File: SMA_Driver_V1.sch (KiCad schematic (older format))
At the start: 70 parts, among them J1 Human_Interface_Tether, J2 RM08V_Conn, Q1 Q_NMOS_GDS, Q2 Q_NMOS_GDS, U1 UDT020A0X3-SRZ, U2 INA332, U3 MCP3208, U4 MicroSD_Breakout_ADF

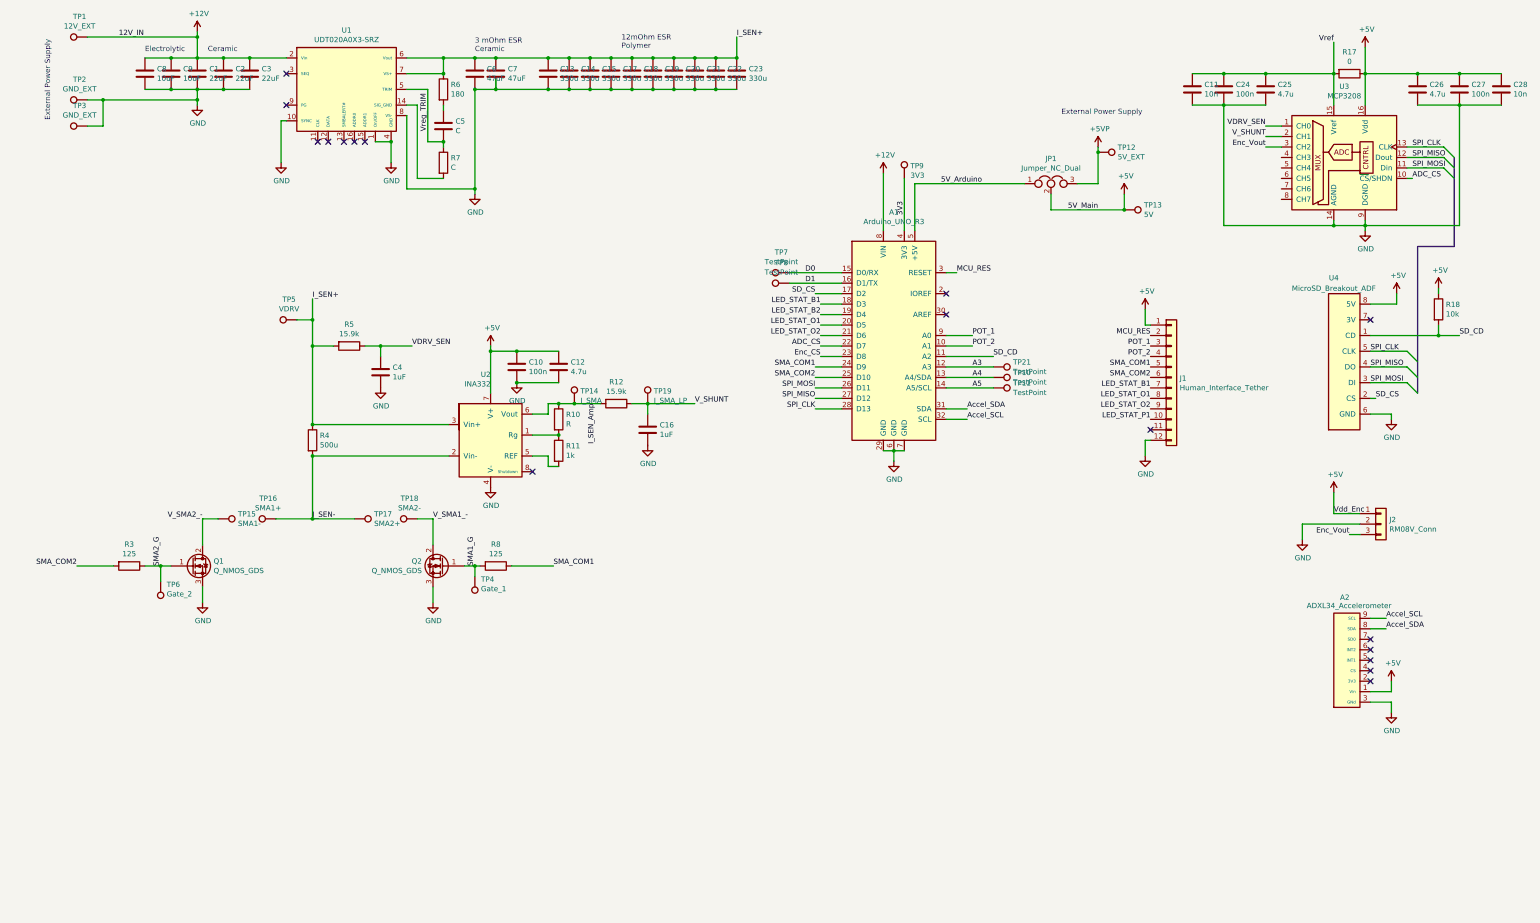
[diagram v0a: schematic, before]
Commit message: fixed notes on 'SMA Driver V1 changes for V2'
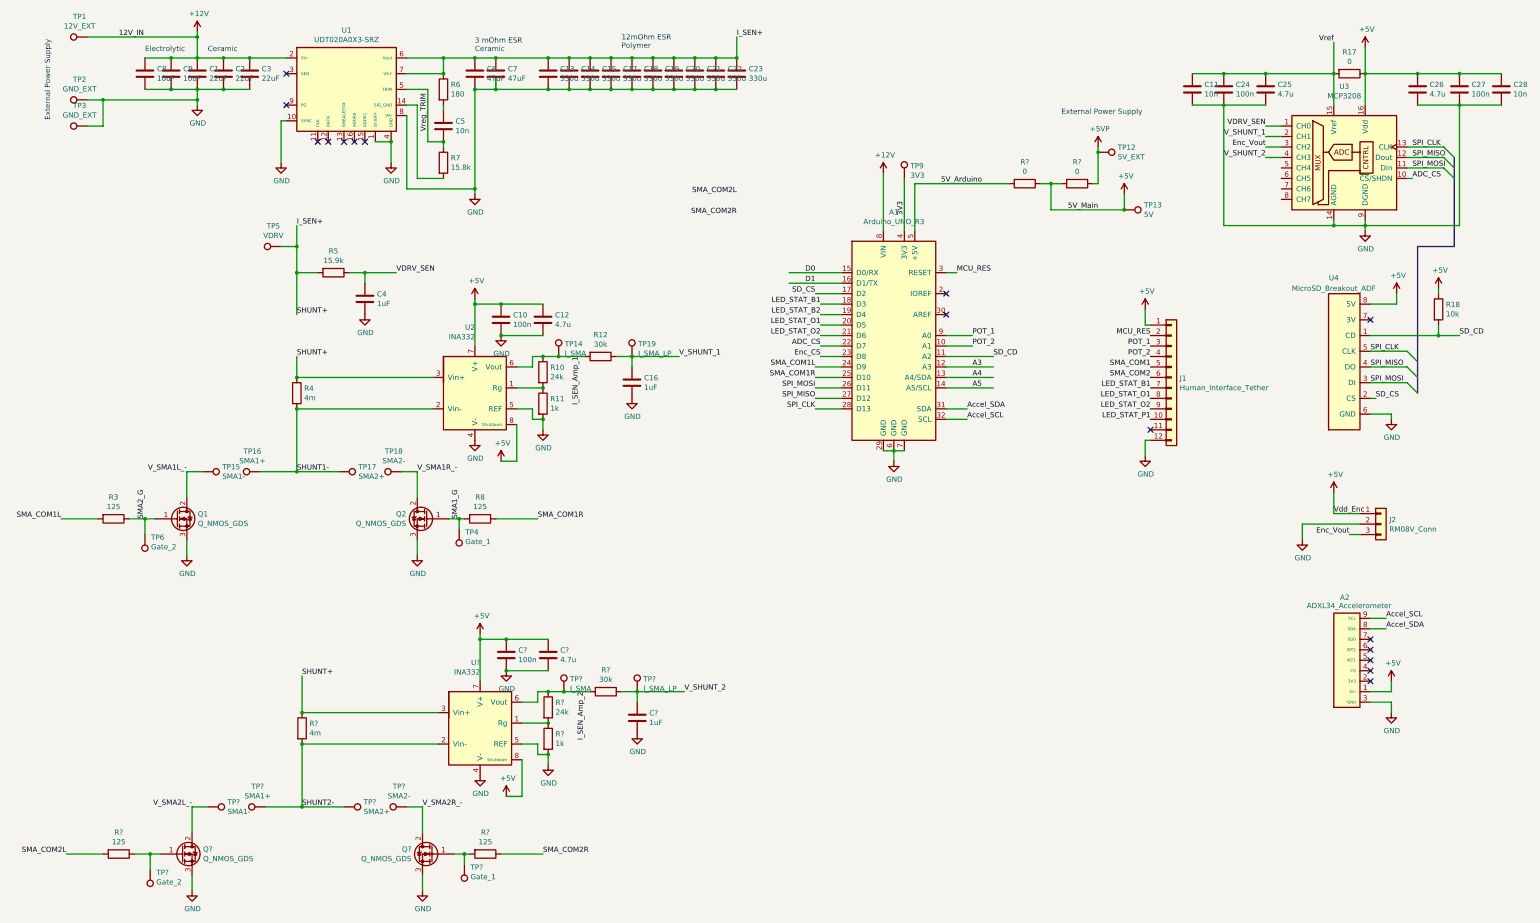
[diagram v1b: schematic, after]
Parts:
- removed JP1: Jumper_NC_Dual, Connector:FanPinHeader_1x03_P2.54mm_Vertical, symbol Device:Jumper_NC_Dual
- removed TP10, TP11, TP21, TP7, TP8: TestPoint, TestPoint:TestPoint_THTPad_D2.0mm_Drill1.0mm, symbol Connector:TestPoint
- added C?: 1uF, Capacitor_SMD:C_0805_2012Metric_Pad1.15x1.40mm_HandSolder, symbol Device:C
- added C?: 100n, Capacitor_SMD:C_0805_2012Metric_Pad1.15x1.40mm_HandSolder, symbol Device:C
- added C?: 4.7u, Capacitor_SMD:C_0805_2012Metric_Pad1.15x1.40mm_HandSolder, symbol Device:C
- added Q? (x2): Q_NMOS_GDS, custom:SO-8FL_v2, symbol Device:Q_NMOS_GDS
- added R? (x2): 0, Resistor_SMD:R_0805_2012Metric, symbol Device:R
- added R?: 4m, Resistor_SMD:R_2512_6332Metric_Pad1.52x3.35mm_HandSolder, symbol Device:R
- added R? (x2): 125, Resistor_SMD:R_0805_2012Metric, symbol Device:R
- added R?: 1k, Resistor_SMD:R_0805_2012Metric, symbol Device:R
- added R?: 24k, Resistor_SMD:R_0805_2012Metric, symbol Device:R
- added R?: 30k, Resistor_SMD:R_0805_2012Metric, symbol Device:R
- added TP?: Gate_2, TestPoint:TestPoint_Loop_D2.60mm_Drill1.6mm_Beaded, symbol Connector:TestPoint
- added TP?: Gate_1, TestPoint:TestPoint_Loop_D2.60mm_Drill1.6mm_Beaded, symbol Connector:TestPoint
- added TP?: I_SMA, TestPoint:TestPoint_Loop_D2.60mm_Drill1.6mm_Beaded, symbol Connector:TestPoint
- added TP?: SMA1-, TestPoint:TestPoint_Plated_Hole_D3.0mm, symbol Connector:TestPoint
- added TP?: SMA2-, TestPoint:TestPoint_Plated_Hole_D3.0mm, symbol Connector:TestPoint
- added TP?: SMA1+, TestPoint:TestPoint_Plated_Hole_D3.0mm, symbol Connector:TestPoint
- added TP?: SMA2+, TestPoint:TestPoint_Plated_Hole_D3.0mm, symbol Connector:TestPoint
- added TP?: I_SMA_LP, TestPoint:TestPoint_Loop_D2.60mm_Drill1.6mm_Beaded, symbol Connector:TestPoint
- added U?: INA332, Package_SO:VSSOP-8_3.0x3.0mm_P0.65mm, symbol SMA_Driver_Components:INA332
- C5: value C -> 10n
- Q1, Q2: footprint custom:SO-8FL -> custom:SO-8FL_v2
- R10: value R -> 24k
- R12: value 15.9k -> 30k
- R4: value 500u -> 4m
- R7: value C -> 15.8k
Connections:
- net +5V: now also U2.8 (Shutdown), C?.1, C?.1, R?.1, R?.2, U?.7 (V+), U?.8 (Shutdown)
- net +5VP: now also R?.1
- net 5V_Arduino: now also R?.2
- net GND: now also R11.2, U2.5 (REF), C?.2, C?.2, C?.2, Q?.3 (S), Q?.3 (S), R?.2, U?.4 (V-), U?.5 (REF)
- net I_SEN+: now also R?.1, U?.3 (Vin+)
- net SMA_COM1: no longer A1.24 (D9), R8.1
- net SMA_COM2: no longer A1.25 (D10), R3.2
- net V_SHUNT_2: now reaches U3.4 (CH3)
- net V_SHUNT_2: now also C?.1, R?.1, TP?.1
- net I_SEN- renamed SHUNT1-
- net I_SEN_Amp renamed I_SEN_Amp_1
- net V_SHUNT renamed V_SHUNT_1
- net V_SMA1_- renamed V_SMA1R_-
- net V_SMA2_- renamed V_SMA1L_-
- new net: Q?.1 (G), R?.1, TP?.1
- new net: Q?.1 (G), R?.2, TP?.1
- new net: R?.1, R?.2, U?.1 (Rg)
- new net I_SEN_Amp_2: R?.1, R?.2, TP?.1, U?.6 (Vout)
- new net SHUNT2-: R?.2, TP?.1, TP?.1, U?.2 (Vin-)
- new net SMA_COM1L: A1.24 (D9), R3.2
- new net SMA_COM1R: A1.25 (D10), R8.1
- new net SMA_COM2L: R?.2
- new net SMA_COM2R: R?.1
- new net V_SMA2L_-: Q?.2 (D), TP?.1
- new net V_SMA2R_-: Q?.2 (D), TP?.1
- no-connect marks 17 -> 16
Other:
- moved on the sheet: C10, C12, C16, C4, Q1, Q2, R10, R11, R12, R3, R4, R5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

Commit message: PCB Rev 2.0 Fixed issues on PCB changes for V2 doc
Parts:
- removed TP17: SMA2+, TestPoint:TestPoint_Plated_Hole_D3.0mm, symbol Connector:TestPoint
- removed TP9: 3V3, TestPoint:TestPoint_THTPad_D2.0mm_Drill1.0mm, symbol Connector:TestPoint
- removed TP?: SMA1+, TestPoint:TestPoint_Plated_Hole_D3.0mm, symbol Connector:TestPoint
- added C32: 10uF, Capacitor_SMD:CP_Elec_5x5.3, symbol Device:C
- added TP22: VREF, TestPoint:TestPoint_Pad_1.5x1.5mm, symbol Connector:TestPoint
- C22: value 330u -> 4.7u; footprint Capacitor_Tantalum_SMD:CP_EIA-7343-43_Kemet-X_Pad2.25x2.55mm_HandSolder -> Capacitor_SMD:C_0805_2012Metric_Pad1.15x1.40mm_HandSolder
- C23: value 330u -> 100n; footprint Capacitor_Tantalum_SMD:CP_EIA-7343-43_Kemet-X_Pad2.25x2.55mm_HandSolder -> Capacitor_SMD:C_0805_2012Metric_Pad1.15x1.40mm_HandSolder
- J1: footprint Connector_Molex:Molex_PicoBlade_53047-2410_1x12_P1.25mm_Vertical -> Connector_Molex:Molex_PicoBlade_53047-2810_1x14_P1.25mm_Vertical; symbol Connector_Generic:Conn_01x12 -> Connector_Generic:Conn_01x14
- J2: footprint Connector_PinHeader_2.54mm:PinHeader_1x03_P2.54mm_Vertical -> Connector_Molex:Molex_PicoBlade_53047-0610_1x03_P1.25mm_Vertical
- gave numbers to parts that had none: 21
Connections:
- net A3 is gone; now on net SD_CD: A1.12 (A3)
- net LED_STAT_P1 is gone; now on net SMA_H2_R: J1.10 (Pin_10)
- net SMA_COM2 is gone; now on net SMA_H1_R: J1.6 (Pin_6)
- net SMA_COM2L is gone; now on net SMA_H2_L: R1.2
- net SMA_COM2R is gone; now on net SMA_H2_R: R9.1
- net +12V: now also C22.1, C23.2, C32.1
- net Enc_Vout: now also U3.8 (CH7); no longer U3.3 (CH2)
- net GND: now also C23.1, J1.14 (Pin_14), C32.2; no longer C23.2, J1.12 (Pin_12)
- net I_SEN+: no longer C22.1, C23.1
- net LED_STAT_B1: now also J1.8 (Pin_8); no longer J1.7 (Pin_7)
- net LED_STAT_B2: now also J1.9 (Pin_9)
- net POT_1: now also A1.10 (A1); no longer A1.9 (A0)
- net POT_2: now also A1.11 (A2); no longer A1.10 (A1)
- net SD_CD: no longer A1.11 (A2)
- net SD_CS: now also A1.9 (A0); no longer A1.17 (D2)
- net V_SHUNT_2: now also U3.3 (CH2); no longer U3.4 (CH3)
- net SMA_H2_L: now reaches J1.11 (Pin_11)
- net SMA_H2_L: now also A1.20 (D5)
- net G_H2_L: now reaches Q3.1 (G), R1.1, TP7.1
- net G_H2_R: now reaches Q4.1 (G), R9.2, TP17.1
- net A4 renamed LED_STAT_O
- net LED_STAT_O: now also J1.7 (Pin_7)
- net A5: no longer names the net of A1.14 (A5/SCL)
- net D0: no longer names the net of A1.15 (D0/RX)
- net D1: no longer names the net of A1.16 (D1/TX)
- net Enc_CS: no longer names the net of A1.23 (D8)
- removed net LED_STAT_O1: A1.20 (D5), J1.8 (Pin_8)
- net LED_STAT_O2 renamed SMA_H2_R
- net SMA_H2_R: no longer J1.9 (Pin_9)
- net SHUNT1- renamed I_SEN1-
- net SHUNT2- renamed I_SEN-
- net SMA1_G renamed G_H1_R
- net SMA2_G renamed G_H1_L
- net SMA_COM1 renamed SMA_H1_L
- net SMA_H1_L: now also A1.25 (D10), R3.2
- net SMA_COM1L renamed SMA_H1_R
- net SMA_H1_R: now also R8.1; no longer R3.2
- removed net SMA_COM1R: A1.25 (D10), R8.1
- net V_SMA1L_- renamed V_H1_L-
- net V_SMA1R_- renamed V_H1_R-
- net V_SMA2L_- renamed V_H2_L-
- net V_SMA2R_- renamed V_H2_R-
- net Vref: no longer names the net of C11.1, C24.1, C25.1, R17.2, U3.15 (Vref)
- net Vref: now also TP22.1
- new net LED_STAT_P: A1.17 (D2), J1.12 (Pin_12)
- no-connect marks 16 -> 24
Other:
- moved on the sheet: TP10, TP16

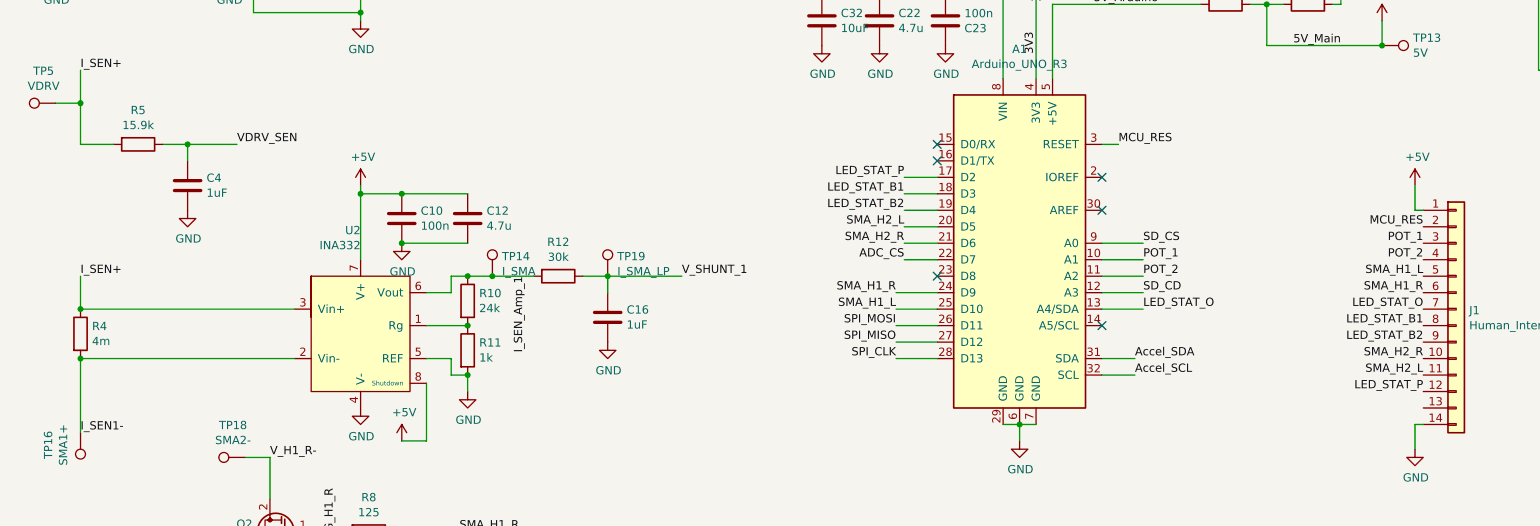
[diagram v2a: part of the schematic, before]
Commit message: added components for button, final draft 1
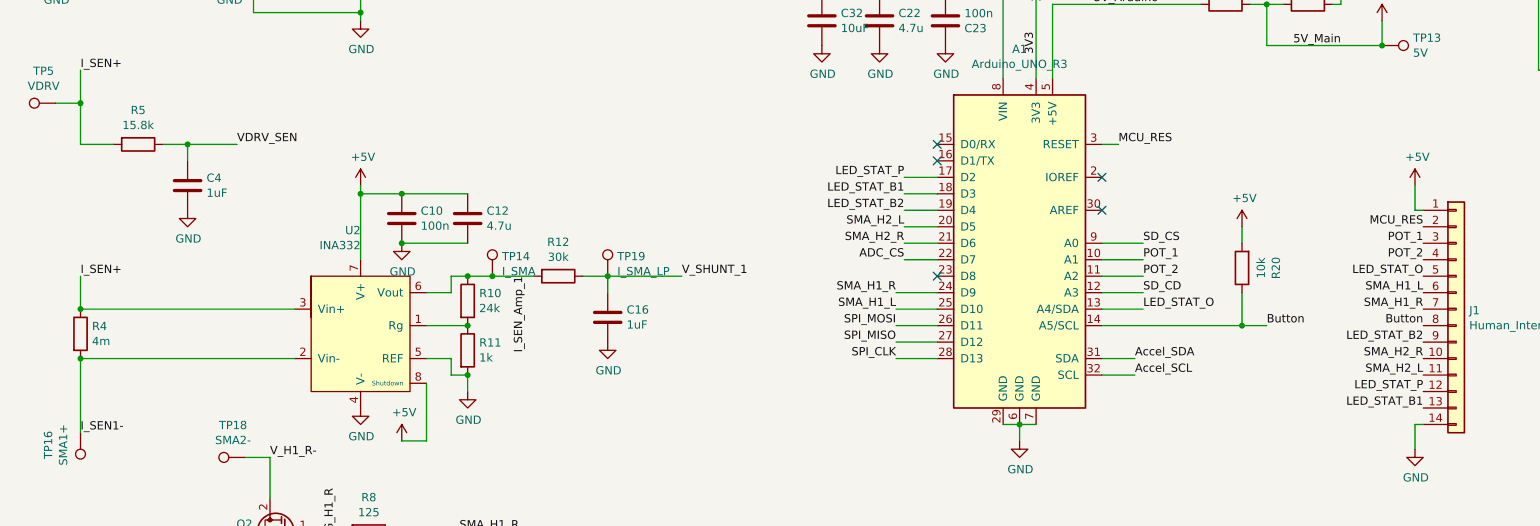
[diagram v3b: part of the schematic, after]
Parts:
- added R20: 10k, Resistor_SMD:R_0805_2012Metric, symbol Device:R
- R5: value 15.9k -> 15.8k
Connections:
- net +5V: now also R20.2
- net LED_STAT_B1: now also J1.13 (Pin_13); no longer J1.8 (Pin_8)
- net LED_STAT_O: now also J1.5 (Pin_5); no longer J1.7 (Pin_7)
- net SMA_H1_L: now also J1.6 (Pin_6); no longer J1.5 (Pin_5)
- net SMA_H1_R: now also J1.7 (Pin_7); no longer J1.6 (Pin_6)
- net Button: now reaches A1.14 (A5/SCL)
- net Button: now also J1.8 (Pin_8), R20.1
- no-connect marks 24 -> 23
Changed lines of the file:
@@
 P 3900 4400
 F 0 "R5" V 3693 4400 50  0000 C CNN
-F 1 "15.9k" V 3784 4400 50  0000 C CNN
+F 1 "15.8k" V 3784 4400 50  0000 C CNN
 F 2 "Resistor_SMD:R_0805_2012Metric" V 3830 4400 50  0001 C CNN
 F 3 "~" H 3900 4400 50  0001 C CNN
@@
 Text Label 11700 5100 2    50   ~ 0
 POT_2
-Text Label 11700 5200 2    50   ~ 0
+Text Label 11700 5300 2    50   ~ 0
 SMA_H1_L
-Text Label 11700 5300 2    50   ~ 0
+Text Label 11700 5400 2    50   ~ 0
 SMA_H1_R
-Text Label 11700 5500 2    50   ~ 0
+Text Label 11700 6000 2    50   ~ 0
 LED_STAT_B1
 Text Label 11700 5600 2    50   ~ 0
@@
 Text Label 11700 5900 2    50   ~ 0
 LED_STAT_P
-Text Label 11700 5400 2    50   ~ 0
+Text Label 11700 5200 2    50   ~ 0
 LED_STAT_O
 Wire Wire Line
@@
 Wire Wire Line
 	8750 4600 8550 4600
-NoConn ~ 9750 5500
 $Comp
 L Device:C C23
@@
 Wire Wire Line
 	8050 3450 8050 3500
-Wire Bus Line
-	14600 3300 14600 4150
-Wire Bus Line
-	14250 4150 14250 5550
 Connection ~ 8400 3450
 $Comp
@@
 	1    0    0    -1
 $EndComp
+Wire Wire Line
+	9750 5500 10600 5500
+Wire Wire Line
+	10600 5500 10600 5300
+$Comp
+L Device:R R20
+U 1 1 5C349DC2
+P 10600 5150
+F 0 "R20" V 10393 5150 50  0000 C CNN
+F 1 "10k" V 10484 5150 50  0000 C CNN
+F 2 "Resistor_SMD:R_0805_2012Metric" V 10530 5150 50  0001 C CNN
+F 3 "~" H 10600 5150 50  0001 C CNN
+	1    10600 5150
+	-1   0    0    1
+$EndComp
+$Comp
+L power:+5V #PWR0138
+U 1 1 5C34A21A
+P 10600 4900
+F 0 "#PWR0138" H 10600 4750 50  0001 C CNN
+F 1 "+5V" H 10615 5073 50  0000 C CNN
+F 2 "" H 10600 4900 50  0001 C CNN
+F 3 "" H 10600 4900 50  0001 C CNN
+	1    10600 4900
+	1    0    0    -1
+$EndComp
+Wire Wire Line
+	10600 4900 10600 5000
+Wire Wire Line
+	10600 5500 10750 5500
+Wire Bus Line
+	14600 3300 14600 4150
+Wire Bus Line
+	14250 4150 14250 5550
+Connection ~ 10600 5500
+Text Label 10750 5500 0    50   ~ 0
+Button
+Text Label 11700 5500 2    50   ~ 0
+Button
 $EndSCHEMATC

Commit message: Final Board V2.0 after run DMC check completed with no errors
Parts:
- R1, R3, R8, R9: value 125 -> 124
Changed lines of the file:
@@
 P 1800 6750
 F 0 "R3" V 1593 6750 50  0000 C CNN
-F 1 "125" V 1684 6750 50  0000 C CNN
+F 1 "124" V 1684 6750 50  0000 C CNN
 F 2 "Resistor_SMD:R_0805_2012Metric" V 1730 6750 50  0001 C CNN
 F 3 "~" H 1800 6750 50  0001 C CNN
@@
 P 5300 6750
 F 0 "R8" V 5093 6750 50  0000 C CNN
-F 1 "125" V 5184 6750 50  0000 C CNN
+F 1 "124" V 5184 6750 50  0000 C CNN
 F 2 "Resistor_SMD:R_0805_2012Metric" V 5230 6750 50  0001 C CNN
 F 3 "~" H 5300 6750 50  0001 C CNN
@@
 P 1850 9950
 F 0 "R1" V 1643 9950 50  0000 C CNN
-F 1 "125" V 1734 9950 50  0000 C CNN
+F 1 "124" V 1734 9950 50  0000 C CNN
 F 2 "Resistor_SMD:R_0805_2012Metric" V 1780 9950 50  0001 C CNN
 F 3 "~" H 1850 9950 50  0001 C CNN
@@
 P 5350 9950
 F 0 "R9" V 5143 9950 50  0000 C CNN
-F 1 "125" V 5234 9950 50  0000 C CNN
+F 1 "124" V 5234 9950 50  0000 C CNN
 F 2 "Resistor_SMD:R_0805_2012Metric" V 5280 9950 50  0001 C CNN
 F 3 "~" H 5350 9950 50  0001 C CNN
@@
 Wire Wire Line
 	10600 5500 10750 5500
-Wire Bus Line
-	14600 3300 14600 4150
-Wire Bus Line
-	14250 4150 14250 5550
 Connection ~ 10600 5500
 Text Label 10750 5500 0    50   ~ 0
@@
 Text Label 11700 5500 2    50   ~ 0
 Button
+Wire Bus Line
+	14600 3300 14600 4150
+Wire Bus Line
+	14250 4150 14250 5550
 $EndSCHEMATC

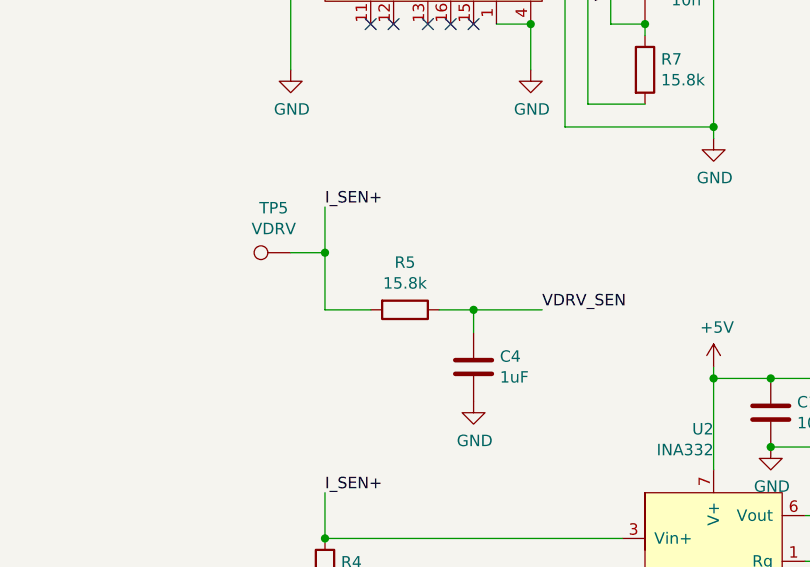
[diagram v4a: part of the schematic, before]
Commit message: changed RC filter for Vin to have same resistor value as amp filter to eliminate common mode noise affecting comparison between Vin and Vshunt in code
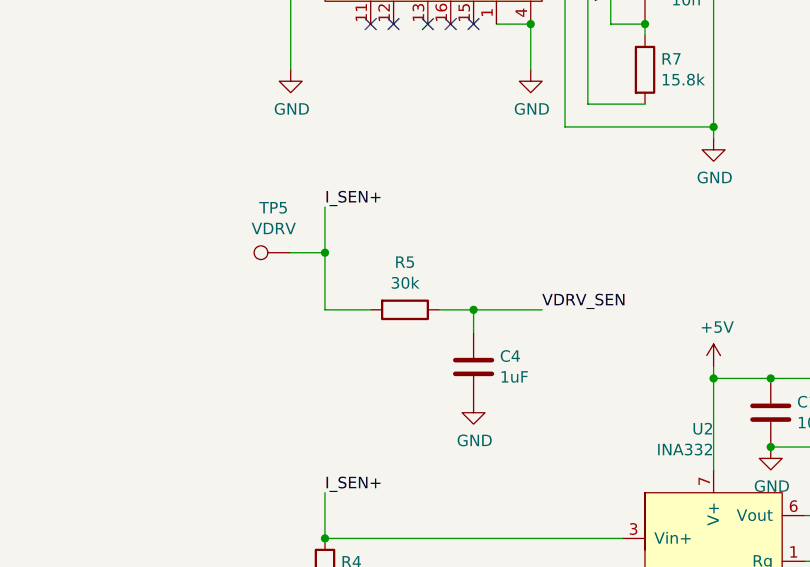
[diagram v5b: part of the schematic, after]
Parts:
- R5: value 15.8k -> 30k
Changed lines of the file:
@@
 P 3900 4400
 F 0 "R5" V 3693 4400 50  0000 C CNN
-F 1 "15.8k" V 3784 4400 50  0000 C CNN
+F 1 "30k" V 3784 4400 50  0000 C CNN
 F 2 "Resistor_SMD:R_0805_2012Metric" V 3830 4400 50  0001 C CNN
 F 3 "~" H 3900 4400 50  0001 C CNN
